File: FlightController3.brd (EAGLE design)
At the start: 50.8 x 86.8 mm, 32 parts, among them U1 NUCLEO_L432KC

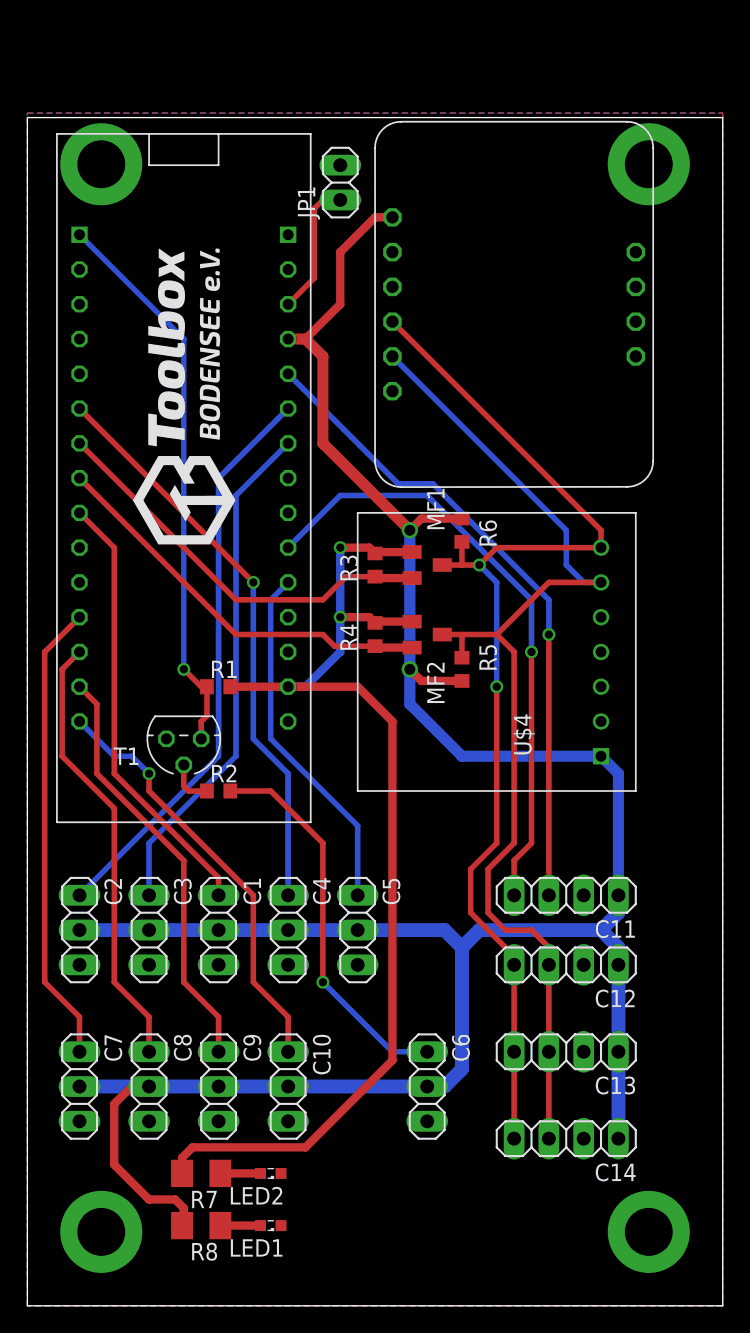
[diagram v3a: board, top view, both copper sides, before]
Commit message: capacitors, dimensions, reset button
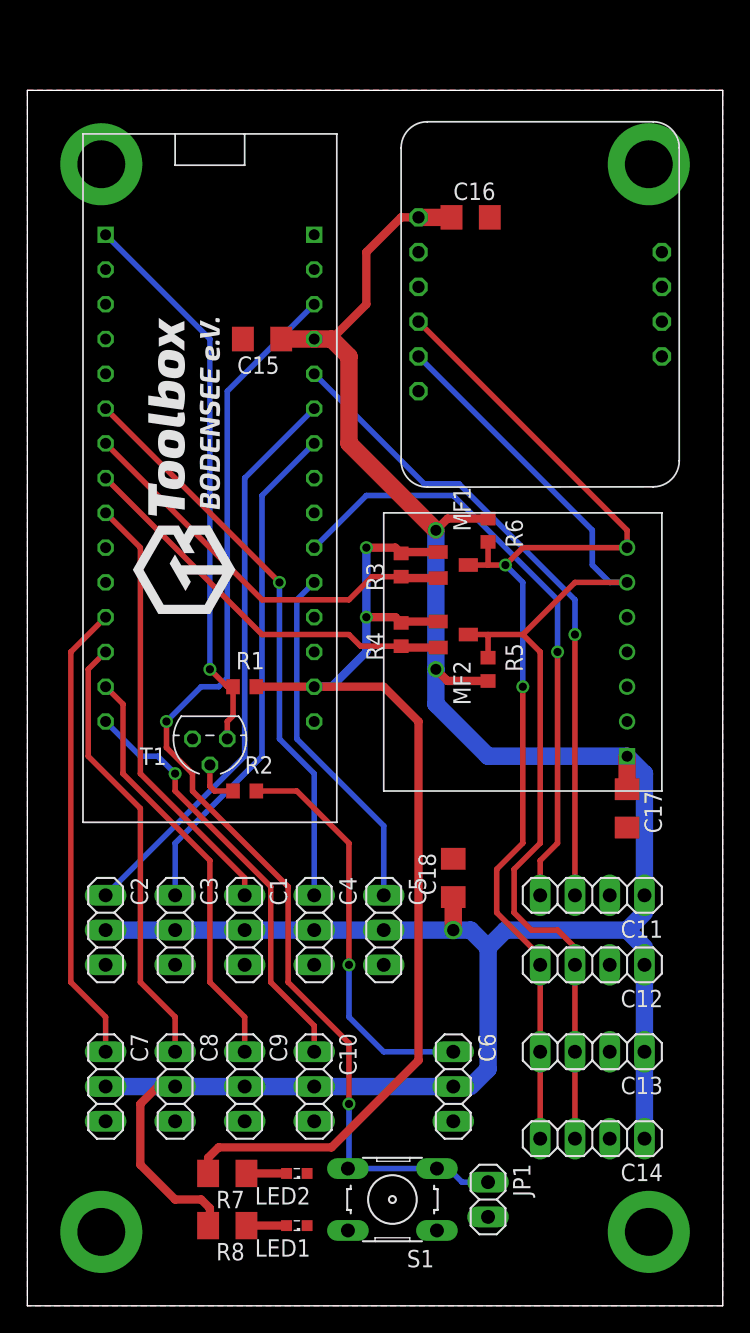
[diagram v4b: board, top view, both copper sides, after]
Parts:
- added C15, C16, C17, C18: 100nF, resistor:C1206
- added S1: (no value), switch-omron:B3F-10XX
- added U$2: TOOLBOX_LOGO, toolbox:TOOLBOX
- moved JP1 75.1 mm to (33.7, -0.64), turned to 270 degrees
- moved U$1 5.08 mm to (12.7, 54.8)
- moved C11 1.91 mm to (41.3, 21.6)
- moved C12 1.91 mm to (41.3, 16.5)
- moved C13 1.91 mm to (41.3, 10.2)
- moved C14 1.91 mm to (41.3, 3.81)
- moved C5 1.91 mm to (26.0, 19.1)
- moved INS1 1.91 mm to (37.5, 64.8)
- moved R3 1.91 mm to (27.3, 45.7)
- moved R4 1.91 mm to (27.3, 40.6)
- moved R5 1.91 mm to (33.7, 38.1)
- moved R6 1.91 mm to (33.7, 48.3)
- moved R7 1.91 mm to (14.6, 1.27)
- moved R8 1.91 mm to (14.6, -2.54)
- moved T1 1.91 mm to (13.3, 33.0)
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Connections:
- net !RST: now also S1.3, S1.4
- net +5V: now also C15.1, C16.1, C17.1, C18.1
- net GND: now also C15.2, C16.2, C17.2, C18.2, S1.1, S1.2
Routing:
- net !RST: track 9.94 -> 84.6 mm, vias 0 -> 2
- net +5V: track 188.5 -> 198.1 mm, vias 2 -> 3
- net SBUS: track 28.2 -> 29.7 mm
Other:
- board size 50.8 x 86.8 mm -> 50.8 x 88.8 mm

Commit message: various improvements, mostly silkscreen labels
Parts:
- C13, C14: value (none) -> I2C
- C2: value AILERON_L -> AILERON L
- C3: value V_TAIL_L -> V-TAIL L
- C4: value V_TAIL_R -> V-TAIL R
- C5: value AILERON_R -> AILERON R
- INS1: value BNO055-BREAKOUT -> BNO055
- JP1, S1: value (none) -> RESET
- LED1: value (none) -> 5V
- LED2: value (none) -> 3V3
- moved R1 1.91 mm to (17.8, 36.8)
- moved C12 0.64 mm to (41.3, 15.9)
- moved C14 0.64 mm to (41.3, 4.45)
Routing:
- net +3V3: track 80.7 -> 78.7 mm
- net !SBUS: track 41.1 -> 42.8 mm
- net SDA5V: track 81.2 -> 80.5 mm
- net +5V: track 198.1 -> 197.5 mm
- net SCL5V: track 79.5 -> 78.9 mm

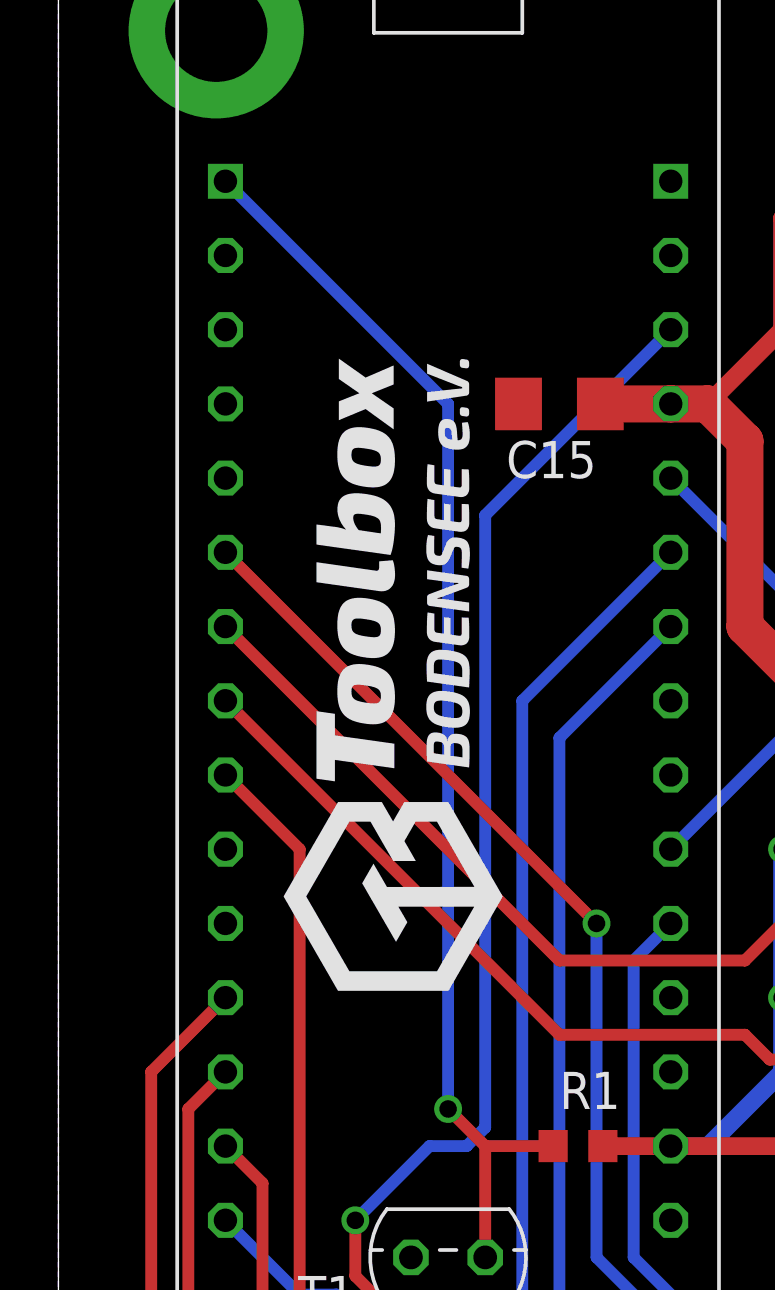
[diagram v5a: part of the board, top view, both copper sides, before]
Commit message: fixed naming of D1/D0 and SBUS connection
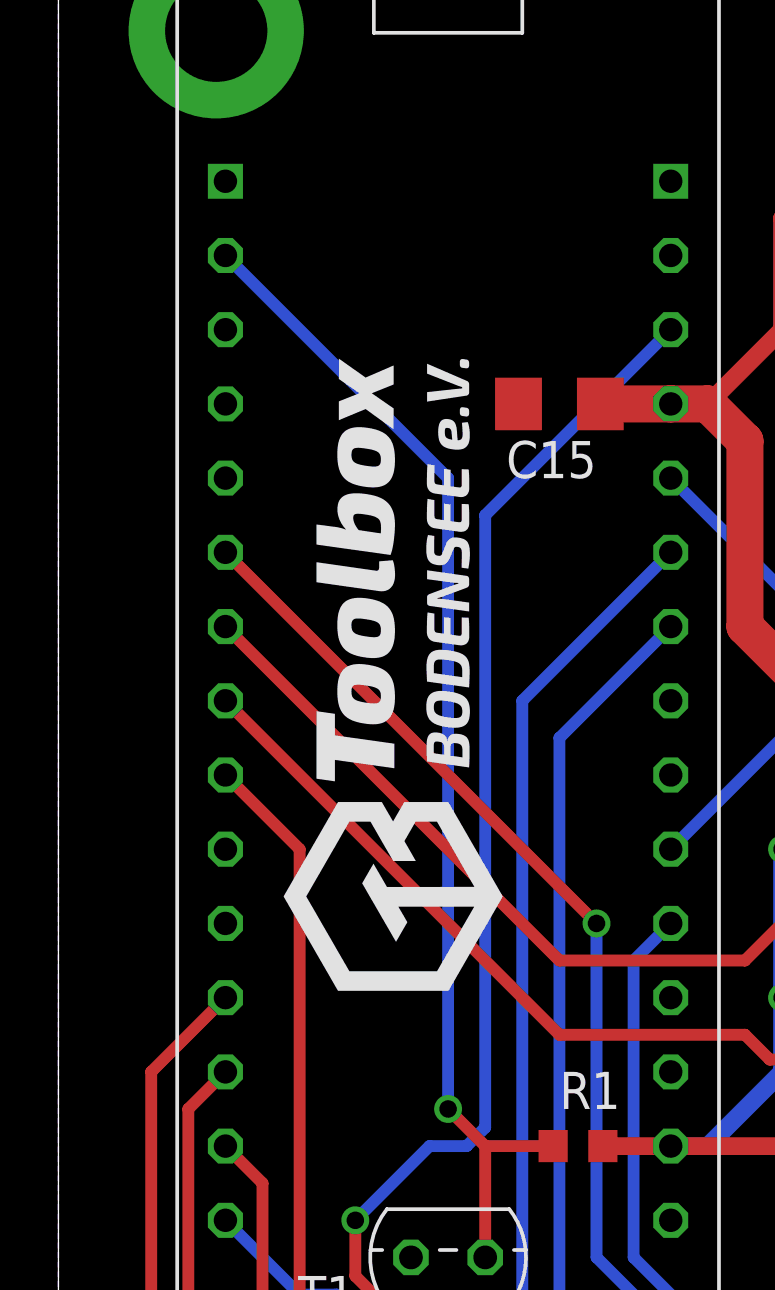
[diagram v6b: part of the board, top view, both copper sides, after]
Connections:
- net !SBUS: now also U1.D0; no longer U1.D1
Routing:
- net !SBUS: track 42.8 -> 40.3 mm
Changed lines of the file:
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@@
 <contactref element="R1" pad="1"/>
 <contactref element="T1" pad="3"/>
-<contactref element="U1" pad="D1"/>
 <wire x1="14.605" y1="36.83" x2="16.93" y2="36.83" width="0.4064" layer="1"/>
 <wire x1="14.605" y1="36.83" x2="13.335" y2="38.1" width="0.4064" layer="1"/>
 <via x="13.335" y="38.1" extent="1-16" drill="0.6" shape="octagon"/>
-<wire x1="13.335" y1="38.1" x2="13.335" y2="62.23" width="0.4064" layer="16"/>
-<wire x1="13.335" y1="62.23" x2="5.715" y2="69.85" width="0.4064" layer="16"/>
+<wire x1="13.335" y1="59.69" x2="13.335" y2="38.1" width="0.4064" layer="16"/>
 <wire x1="14.605" y1="33.02" x2="14.605" y2="36.83" width="0.4064" layer="1"/>
+<contactref element="U1" pad="D0"/>
+<wire x1="5.715" y1="67.31" x2="13.335" y2="59.69" width="0.4064" layer="16"/>
 </signal>
 <signal name="N$1">

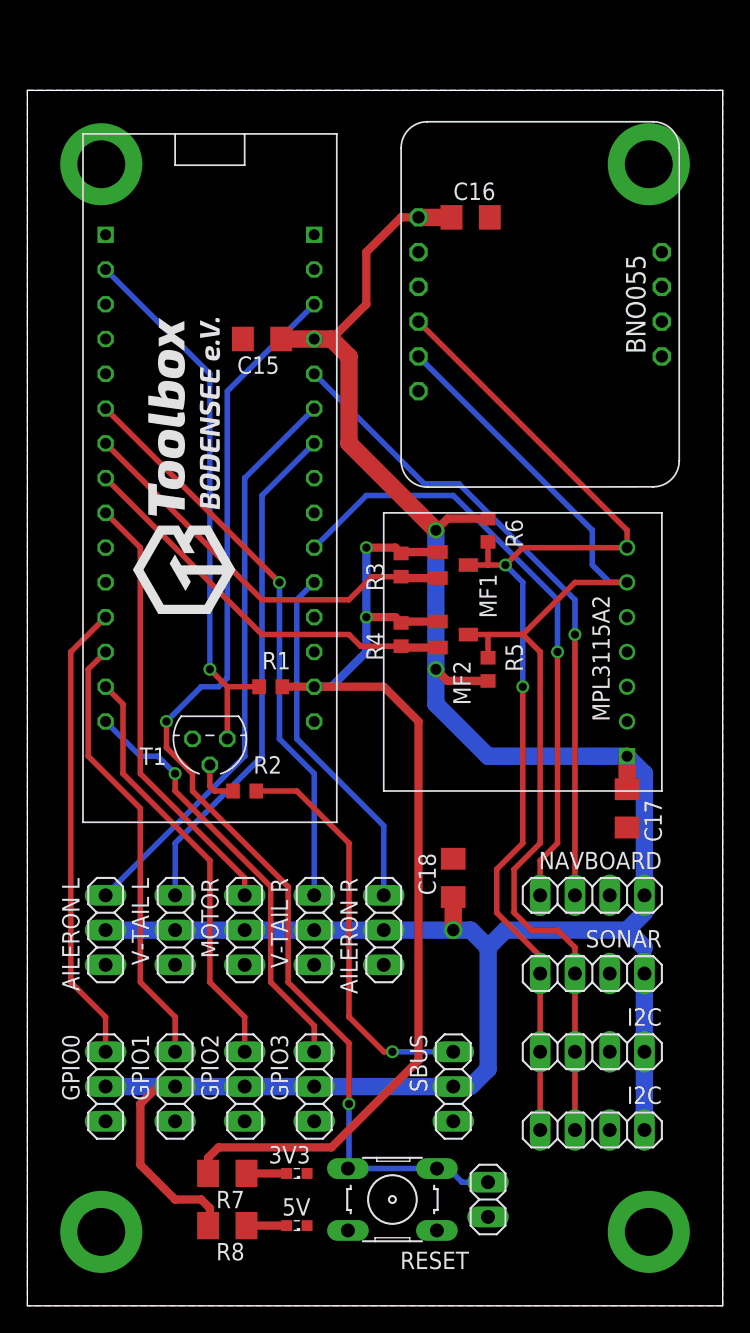
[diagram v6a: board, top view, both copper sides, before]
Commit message: removed GPIO, I2C Ports, added expansion port
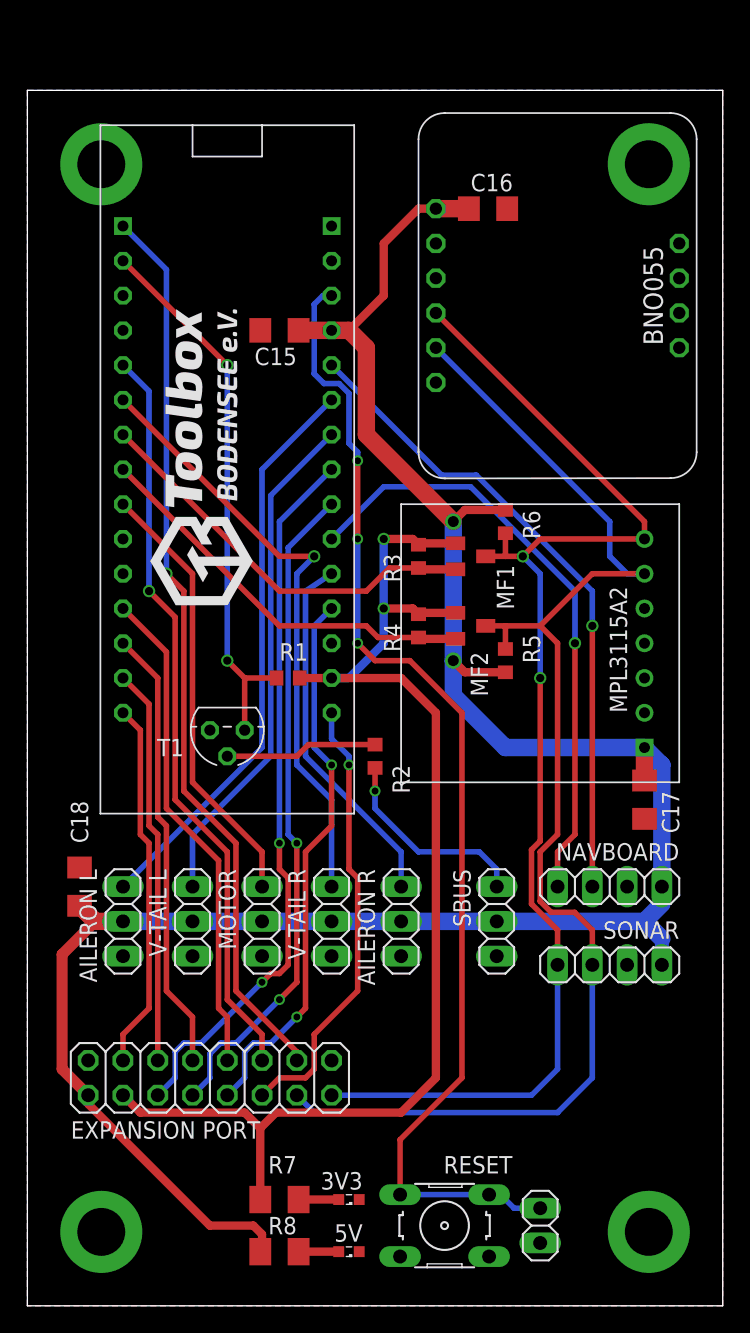
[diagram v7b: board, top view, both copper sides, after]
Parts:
- removed C10: GPIO3, pinhead:1X03
- removed C13, C14: I2C, pinhead:1X04
- removed C7: GPIO0, pinhead:1X03
- removed C8: GPIO1, pinhead:1X03
- removed C9: GPIO2, pinhead:1X03
- added JP2: EXPANSION PORT, pinhead:2X08
- moved C18 27.3 mm to (3.81, 22.2)
- moved C6 12.5 mm to (34.3, 19.7)
- moved R2 9.86 mm to (25.4, 31.8), turned to 270 degrees
- moved JP1 4.26 mm to (37.5, -2.54)
- moved LED1 4.26 mm to (23.5, -4.45)
- moved LED2 4.26 mm to (23.5, -0.64)
- moved R7 4.26 mm to (18.4, -0.64)
- moved R8 4.26 mm to (18.4, -4.45)
- moved S1 4.26 mm to (30.5, -2.54)
- moved U$4 1.42 mm to (37.5, 40.0)
- moved C11 1.42 mm to (42.5, 22.2)
- moved C12 1.42 mm to (42.5, 16.5)
- moved C15 1.42 mm to (18.4, 62.9)
- moved C17 1.42 mm to (45.1, 28.6)
- moved C4 1.42 mm to (22.2, 19.7)
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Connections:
- removed net GPIO0: C7.1, U1.D9
- removed net GPIO1: C8.1, U1.D10
- removed net GPIO2: C9.1, U1.D11
- removed net GPIO3: C10.1, U1.D12
- new net A0: JP2.9, U1.A0
- new net A3: JP2.7, U1.A3
- new net A4: JP2.5, U1.A4
- new net D1: JP2.14, U1.D1
- new net D10: JP2.8, U1.D10
- new net D11: JP2.6, U1.D11
- new net D12: JP2.4, U1.D12
- new net D13: JP2.11, U1.D13
- new net D2: JP2.12, U1.D2
- new net D9: JP2.10, U1.D9
- net +3V3: now also JP2.3
- net +5V: now also JP2.1; no longer C10.2, C13.1, C14.1, C7.2, C8.2, C9.2
- net GND: now also JP2.2; no longer C10.3, C13.2, C14.2, C7.3, C8.3, C9.3
- net SCL5V: now also JP2.13; no longer C13.3, C14.3
- net SDA5V: now also JP2.15; no longer C13.4, C14.4
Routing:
- net D1: track 0.00 -> 66.2 mm, vias 0 -> 1
- net D2: track 0.00 -> 55.0 mm, vias 0 -> 1
- net A4: track 0.00 -> 52.6 mm, vias 0 -> 2
- net A3: track 0.00 -> 48.6 mm, vias 0 -> 2
- net A0: track 0.00 -> 40.5 mm, vias 0 -> 2
- net D9: track 0.00 -> 36.2 mm
- net GPIO0: track 33.9 -> 0.00 mm
- net D13: track 0.00 -> 32.7 mm, vias 0 -> 1
- net D10: track 0.00 -> 32.6 mm
- net GPIO1: track 32.4 -> 0.00 mm
- net GPIO3: track 31.2 -> 0.00 mm, vias 1 -> 0
- net GPIO2: track 30.9 -> 0.00 mm
- net +5V: track 197.5 -> 166.8 mm, vias 3 -> 2
- net D11: track 0.00 -> 29.0 mm
- net D12: track 0.00 -> 27.0 mm
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
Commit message: smaller board footprint, added reset to port
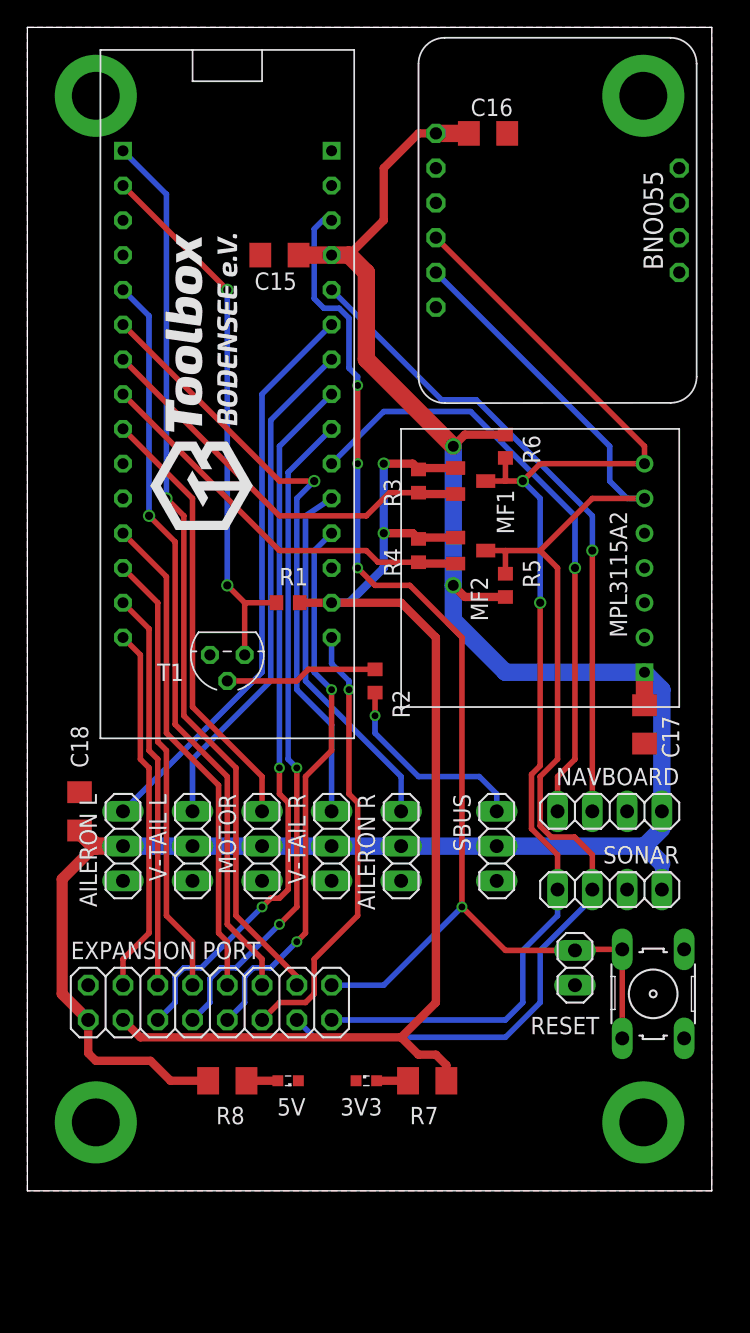
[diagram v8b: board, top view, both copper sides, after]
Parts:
- moved S1 22.8 mm to (45.7, 14.4), turned to 270 degrees
- moved JP1 19.0 mm to (40.0, 16.3)
- moved R7 13.8 mm to (29.2, 8.04), turned to 0 degrees
- moved LED1 13.3 mm to (19.1, 8.04)
- moved R8 13.1 mm to (14.6, 8.04)
- moved LED2 8.77 mm to (24.8, 8.04), turned to 0 degrees
- moved C17 5.50 mm to (45.1, 34.1)
- moved C1 5.50 mm to (17.1, 25.2)
- moved C11 5.50 mm to (42.5, 27.7)
- moved C12 5.50 mm to (42.5, 22.0)
- moved C16 5.50 mm to (33.7, 77.3)
- moved C18 5.50 mm to (3.81, 27.7)
- moved C2 5.50 mm to (6.99, 25.2)
- moved C3 5.50 mm to (12.1, 25.2)
- moved C4 5.50 mm to (22.2, 25.2)
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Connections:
- net !RST: now also JP2.16
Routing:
- net +5V: track 166.8 -> 160.2 mm
- net !RST: track 85.7 -> 89.1 mm, vias 3 -> 4
- net SCL5V: track 98.3 -> 96.0 mm
- net SDA5V: track 93.0 -> 91.9 mm
- net +3V3: track 91.8 -> 90.9 mm
- net N$2: track 2.93 -> 2.29 mm
- net N$3: track 2.93 -> 2.30 mm
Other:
- board size 50.8 x 88.8 mm -> 50 x 85 mm
